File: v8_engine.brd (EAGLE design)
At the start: 100 x 80 mm, 79 parts, among them IC1 4024N, IC2 4046N, IC3 40106N, IC4 LM358N, IC5 LM358N, IC6 LM358N

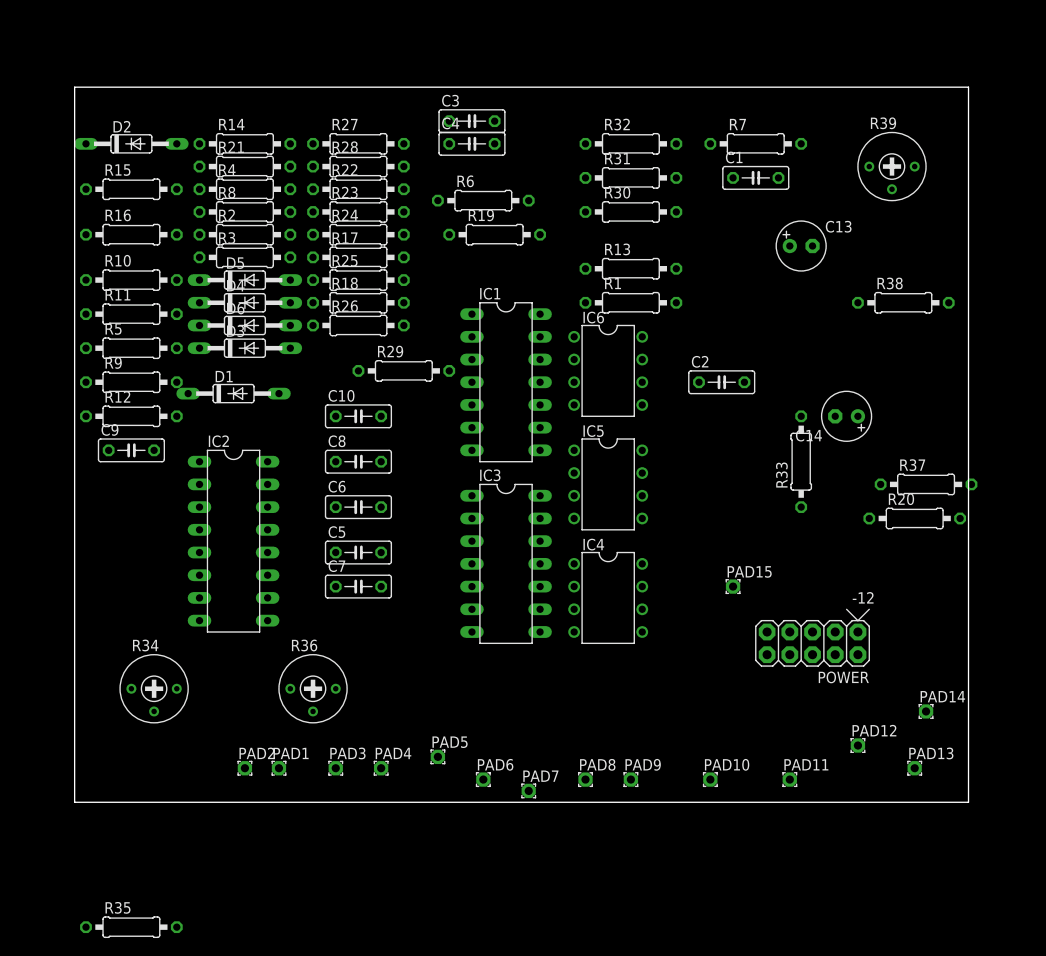
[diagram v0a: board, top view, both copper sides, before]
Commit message: Rearrange all components on the PCB
- Arrange components on pcb to make some kind of sense.
- Change size of board and add screw holes for m3 screw.
	- Note that size/layout might not be final.
- Invoke all ICs to connect them to +12V -12V and GND nets.
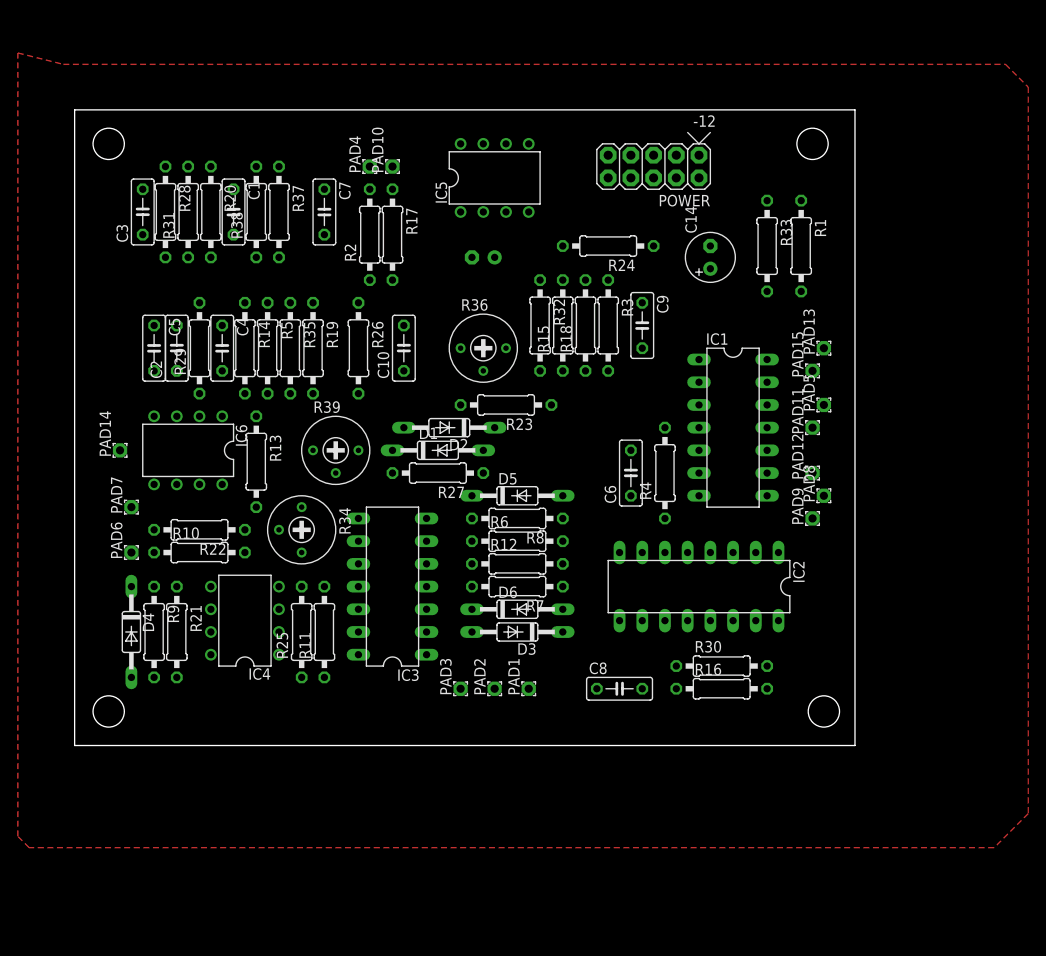
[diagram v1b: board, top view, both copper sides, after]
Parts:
- moved PAD14 94.8 mm to (5.08, 39.4), turned to 90 degrees
- moved R20 85.9 mm to (15.2, 66.0), turned to 270 degrees
- moved R16 83.3 mm to (72.4, 12.7)
- moved R37 78.5 mm to (22.9, 66.0), turned to 270 degrees
- moved PAD10 77.3 mm to (35.6, 71.1), turned to 90 degrees
- moved R38 73.1 mm to (20.3, 66.0), turned to 90 degrees
- moved R39 69.9 mm to (29.2, 39.4)
- moved PAD4 67.3 mm to (33.0, 71.1), turned to 90 degrees
- moved R35 67.2 mm to (24.1, 50.8), turned to 270 degrees
- moved C2 61.1 mm to (11.4, 50.8), turned to 90 degrees
- moved C9 58.8 mm to (63.5, 53.3), turned to 270 degrees
- moved C1 58.5 mm to (17.8, 66.0), turned to 270 degrees
- moved PAD5 58.4 mm to (83.8, 44.5), turned to 90 degrees
- moved R4 56.7 mm to (66.0, 36.8), turned to 90 degrees
- moved R7 56.3 mm to (49.5, 24.1), turned to 180 degrees
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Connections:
- removed net V+: IC4.8, IC5.8, IC6.8
- removed net V-: IC4.4, IC5.4, IC6.4
- removed net VDD: IC1.14, IC2.16, IC3.14
- removed net VSS: IC1.7, IC2.8, IC3.7
- net +12V: now also IC1.14, IC2.16, IC3.14, IC4.8, IC5.8, IC6.8
- net -12V: now also IC3.7, IC4.4, IC5.4, IC6.4
- net GND: now also IC1.7, IC2.8
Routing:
- added copper zone on layer 1, net GND
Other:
- board size 100 x 80 mm -> 87.3 x 71.1 mm

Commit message: Change big ICs from DIL to SO make board smaller and start routing
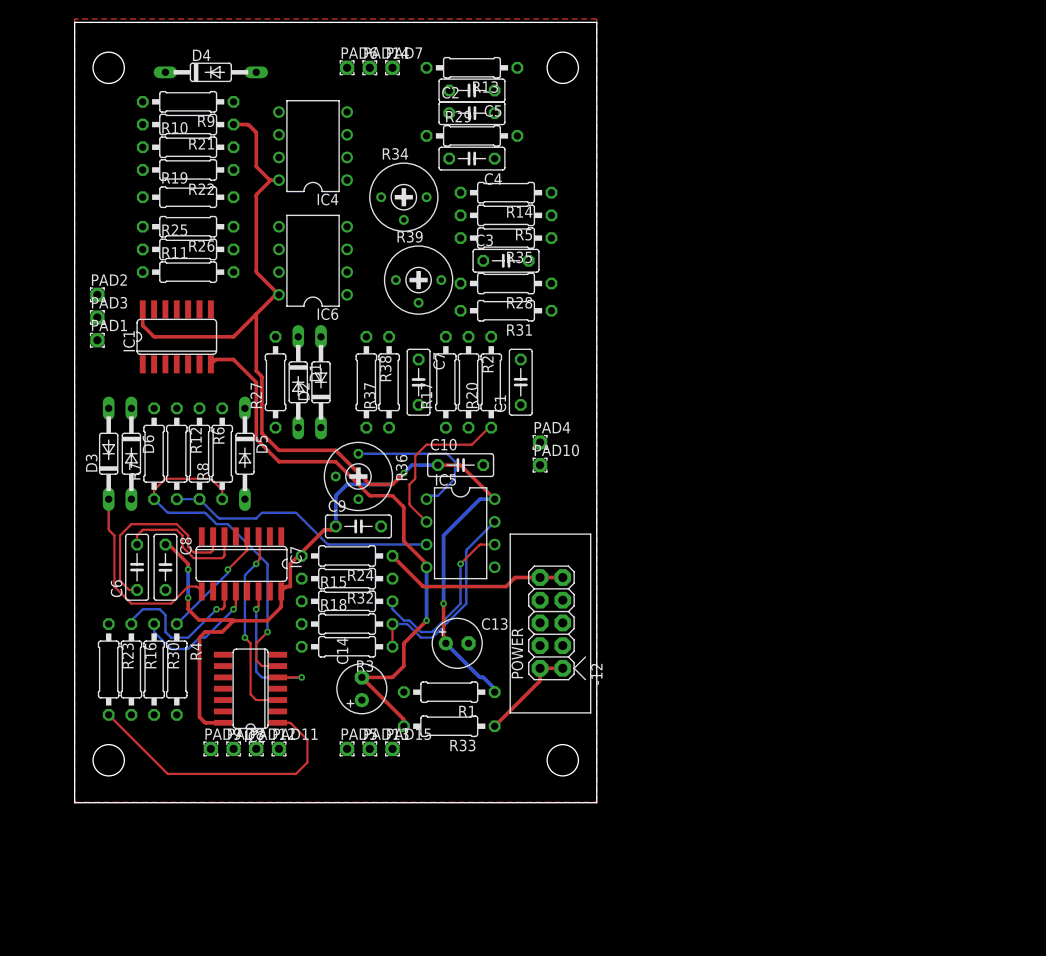
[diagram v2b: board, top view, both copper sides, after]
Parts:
- removed IC3: 40106N, 40xx:DIL14
- added IC7: 4046D, 40xx:SO16
- IC1: value 4024N -> 40106D; device 40xx:DIL14 -> 40xx:SO14
- IC2: value 4046N -> 4024D; device 40xx:DIL16 -> 40xx:SO14
- moved PAD9 72.1 mm to (15.2, 5.97), turned to 0 degrees
- moved PAD8 71.9 mm to (17.8, 5.97), turned to 0 degrees
- moved PAD11 69.7 mm to (22.9, 5.97), turned to 0 degrees
- moved PAD12 69.5 mm to (20.3, 5.97), turned to 0 degrees
- moved PAD13 67.8 mm to (33.0, 5.97), turned to 0 degrees
- moved R16 66.1 mm to (6.35, 14.9), turned to 270 degrees
- moved PAD5 65.8 mm to (30.5, 5.97), turned to 0 degrees
- moved R33 64.4 mm to (41.9, 8.51), turned to 180 degrees
- moved R1 63.6 mm to (41.9, 12.3), turned to 180 degrees
- moved R30 63.5 mm to (8.89, 14.9), turned to 270 degrees
- moved D4 63.2 mm to (15.2, 81.7), turned to 0 degrees
- moved PAD15 63.2 mm to (35.6, 5.97), turned to 0 degrees
- moved IC1 63.1 mm to (11.4, 52.1), turned to 0 degrees
- moved PAD2 62.6 mm to (2.54, 56.8), turned to 0 degrees
- moved C14 62.0 mm to (32.1, 12.7)
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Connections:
- net +12V: now also IC2.14, IC7.16; no longer IC2.16, IC3.14
- net -12V: now also IC1.7; no longer IC3.7
- net C_IN: now also IC7.3; no longer IC1.3
- net C_OUT: now also IC1.1, IC7.2; no longer IC2.2, IC3.1
- net GND: now also IC2.2, IC2.7, IC7.5, IC7.8; no longer IC1.2, IC1.7, IC2.5, IC2.8
- net LEFT_CH: now also IC1.3; no longer IC3.3
- net N$1: now also IC7.4; no longer IC2.4
- net N$10: now also IC1.9; no longer IC3.9
- net N$16: now also IC7.7; no longer IC2.7
- net N$17: now also IC7.6; no longer IC2.6
- net N$18: now also IC7.11; no longer IC2.11
- net N$19: now also IC7.12; no longer IC2.12
- net N$21: now also IC2.1; no longer IC1.1
- net N$22: now also IC2.6; no longer IC1.6
- net N$24: now also IC1.4; no longer IC3.4
- net N$26: now also IC1.2; no longer IC3.2
- net N$41: now also IC1.6; no longer IC3.6
- net N$48: now also IC1.11, IC7.9; no longer IC2.9, IC3.11
- net N$6: now also IC1.8; no longer IC3.8
- net N$8: now also IC1.10; no longer IC3.10
- net RIGHT_CH: now also IC1.5; no longer IC3.5
- net SIG_IN: now also IC2.5, IC7.14; no longer IC1.5, IC2.14
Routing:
- net +12V: track 0.00 -> 177.5 mm, vias 0 -> 4
- net -12V: track 0.00 -> 64.8 mm, vias 0 -> 1
- net N$22: track 0.00 -> 40.3 mm, vias 0 -> 1
- net N$21: track 0.00 -> 32.1 mm
- net N$25: track 0.00 -> 30.5 mm
- net N$33: track 0.00 -> 23.4 mm
- net N$16: track 0.00 -> 22.0 mm
- net C_IN: track 0.00 -> 22.0 mm, vias 0 -> 2
- net N$48: track 0.00 -> 21.6 mm
- net N$3: track 0.00 -> 20.9 mm
- net N$32: track 0.00 -> 20.0 mm, vias 0 -> 1
- net N$27: track 0.00 -> 18.2 mm
- net N$29: track 0.00 -> 17.1 mm
- net N$18: track 0.00 -> 16.9 mm, vias 0 -> 1
- net SIG_IN: track 0.00 -> 16.3 mm, vias 0 -> 2
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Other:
- board size 87.3 x 71.1 mm -> 58.4 x 87.3 mm

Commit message: Complete routing
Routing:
- net N$41: track 0.00 -> 84.0 mm, vias 0 -> 2
- net N$48: track 21.6 -> 96.0 mm, vias 0 -> 1
- net N$5: track 0.00 -> 70.1 mm, vias 0 -> 2
- net N$37: track 0.00 -> 64.8 mm, vias 0 -> 2
- net -12V: track 64.8 -> 118.3 mm, vias 1 -> 2
- net N$29: track 17.1 -> 69.6 mm, vias 0 -> 4
- net N$38: track 0.00 -> 42.3 mm
- net N$30: track 0.00 -> 40.3 mm
- net C_OUT: track 0.00 -> 32.1 mm, vias 0 -> 2
- net N$43: track 0.00 -> 31.0 mm, vias 0 -> 2
- net N$11: track 0.00 -> 30.4 mm
- net N$10: track 0.00 -> 29.3 mm, vias 0 -> 2
- net N$23: track 0.00 -> 25.8 mm
- net N$46: track 0.00 -> 24.2 mm
- net N$32: track 20.0 -> 44.0 mm
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
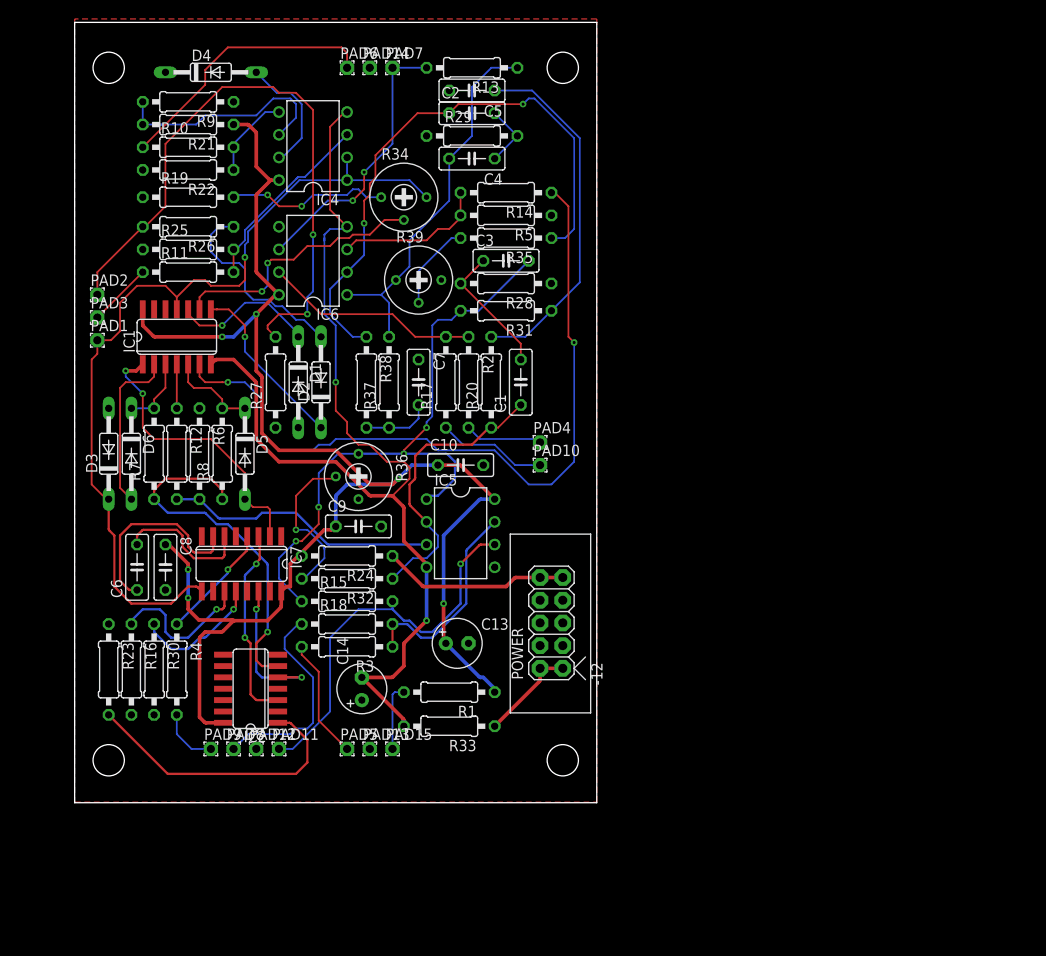
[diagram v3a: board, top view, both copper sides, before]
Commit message: Clean up silk screen and fix issues
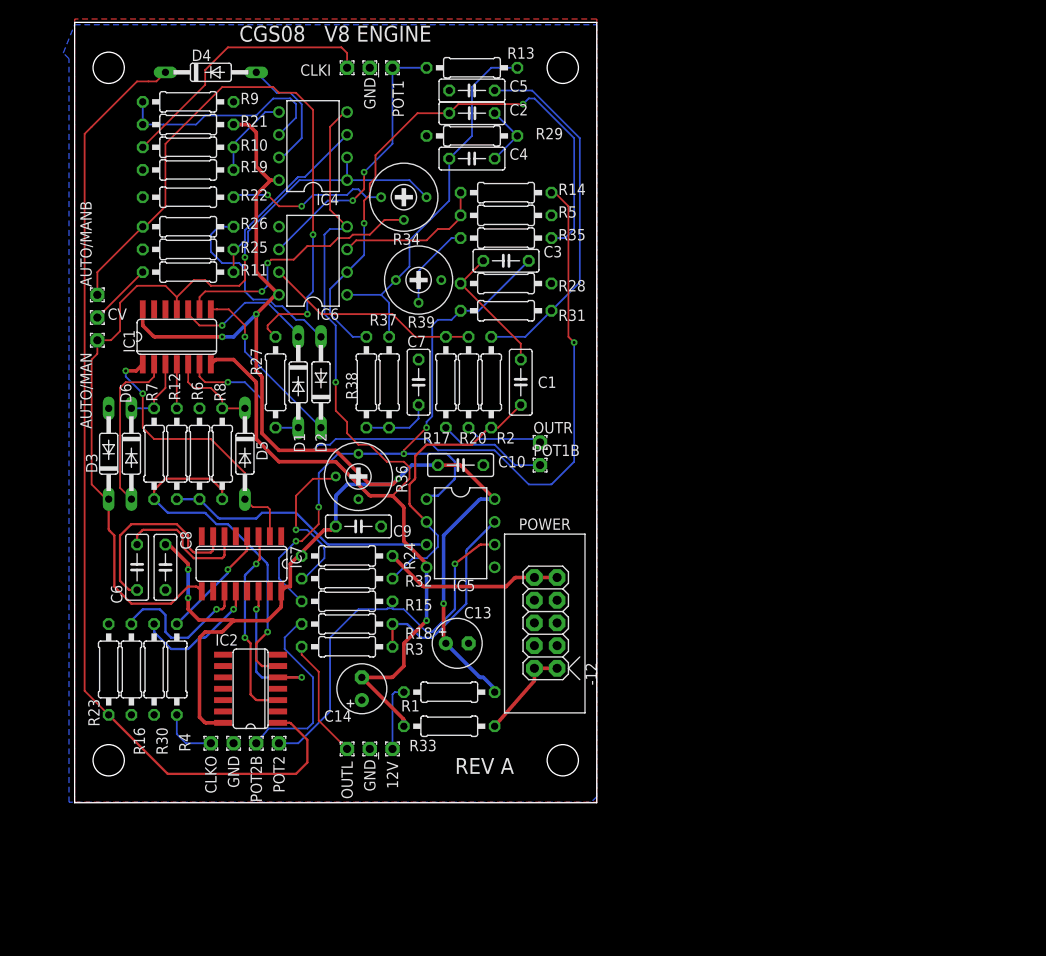
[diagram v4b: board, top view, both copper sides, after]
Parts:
- removed PAD11, PAD8: POT2, wirepad:1,6/0,9
- removed PAD12: GND, wirepad:1,6/0,9
- removed PAD9: CLKO, wirepad:1,6/0,9
- added CLKO: CLKO, wirepad:1,6/0,9
- added GND: GND, wirepad:1,6/0,9
- added POT2: POT2, wirepad:1,6/0,9
- added POT2B: POT2B, wirepad:1,6/0,9
- AUTO/MANB: value AUTO/MAN -> AUTO/MANB
- POT1B: value POT1 -> POT1B
- moved POWER 0.64 mm to (52.7, 20.1)
- renumbered PAD1 to AUTO/MAN, PAD10 to POT1B, PAD13 to GND_, PAD14 to GND__, PAD15 to 12V, PAD2 to AUTO/MANB, PAD3 to CV, PAD4 to OUTR, PAD5 to OUTL, PAD6 to CLKI, PAD7 to POT1
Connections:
- net CLKO: now also CLKO.1; no longer PAD9.1
- net GND: now also GND.1; no longer PAD12.1
- net N$21: now also D4.C
- net N$32: now also POT2.1; no longer PAD11.1
- net N$34: now also POT2B.1; no longer PAD8.1
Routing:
- net N$21: track 32.1 -> 110.1 mm
- net N$34: track 23.5 -> 20.8 mm
- net SIG_IN: track 16.3 -> 19.0 mm
- net N$2: track 0.00 -> 2.54 mm
- net N$3: track 20.9 -> 20.2 mm
- added copper zone on layer 16, net N$9
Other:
- board text added: "CGS08 V8 ENGINE"
- board text added: "Copyright 2018 by Martin Eriksson"
- board text added: "Original design by Ken Stone cgs.synth.net/modules/v8.html"
- board text added: "REV A"
